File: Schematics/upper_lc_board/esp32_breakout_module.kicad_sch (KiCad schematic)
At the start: 28 parts, among them J1 USB_C_Female_USB2_Small, Q4 2N7002, SW1 SW_ESP_BOOT_MODE, SW2 SW_ESP_RESET, U1 ESP32-S3-WROOM-1-N16, U2 ISO1044BDR

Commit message: final upper control board
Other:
- moved on the sheet: C4, SW1, SW2

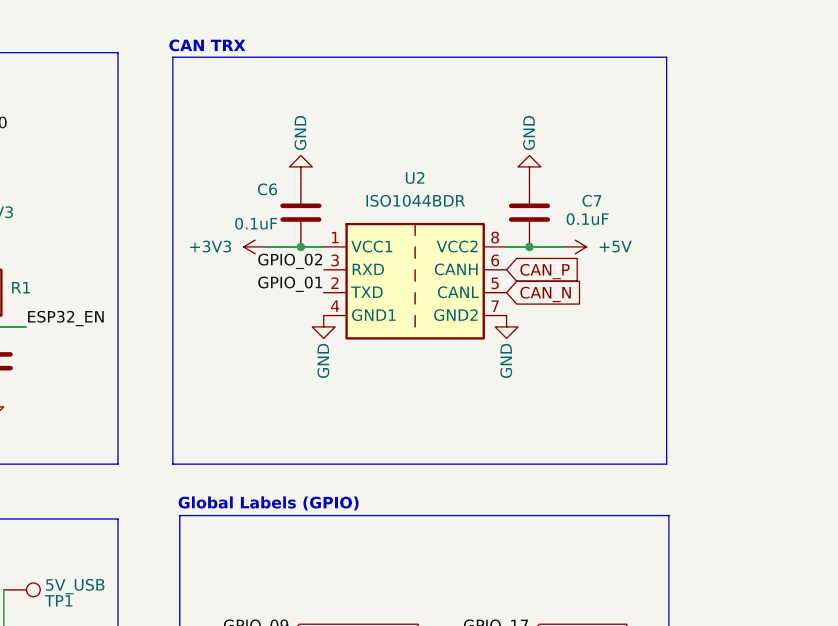
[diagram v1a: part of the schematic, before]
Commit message: final upper control board in cart, fixed HALL connector
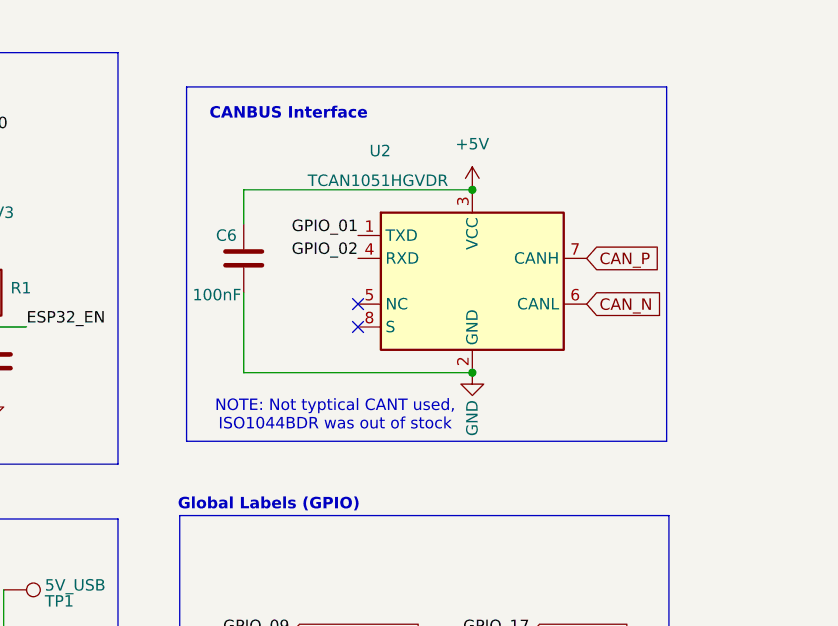
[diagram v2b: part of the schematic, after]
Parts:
- removed C7: 0.1uF, Capacitor_SMD:C_0603_1608Metric, symbol Device:C
- removed U2: ISO1044BDR, ul_ISO1044BDR:SOIC127P600X175-8N, symbol Interface_CAN_LIN:ISO1044BD
- added U2: TCAN1051HGVDR, ul_ISO1044BDR:SOIC_1044BDR_TEX, symbol Interface_CAN_LIN:TCAN330
- C6: value 0.1uF -> 100nF
- U1: Digikey (none) -> 5407-ESP32-S3-WROOM-1-N16CT-ND; LCSC C2913199 -> (none)
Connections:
- net +3V3: no longer C6.1
- net +5V: now also C6.2, U2.3 (VCC)
- net CAN_N: now also U2.6 (CANL)
- net CAN_P: now also U2.7 (CANH)
- net GND: now also C6.1, U2.2 (GND); no longer C6.2
- net GPIO_01: now also U2.1 (TXD)
- net GPIO_02: now also U2.4 (RXD)
- no-connect marks 13 -> 15
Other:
- note added: "CANBUS Interface"
- note added: "NOTE: Not typtical CANT used, ISO1044BDR was out of stock"
- note removed: "CAN TRX"

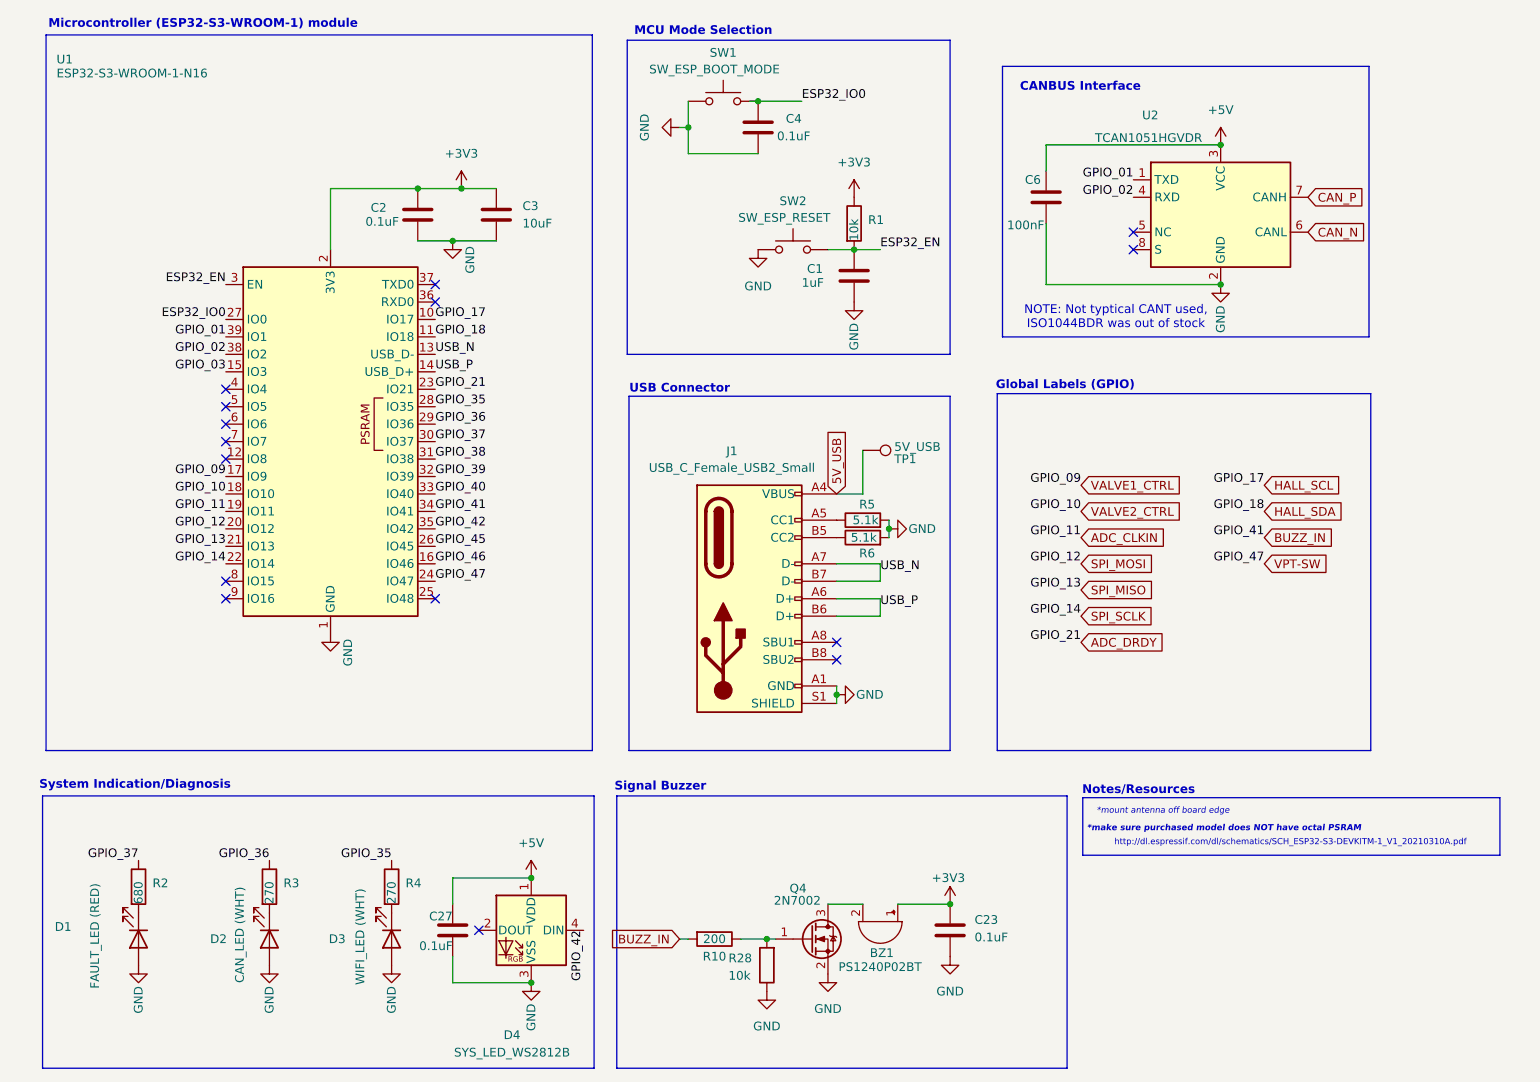
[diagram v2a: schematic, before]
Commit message: added 24V sensing to upper board
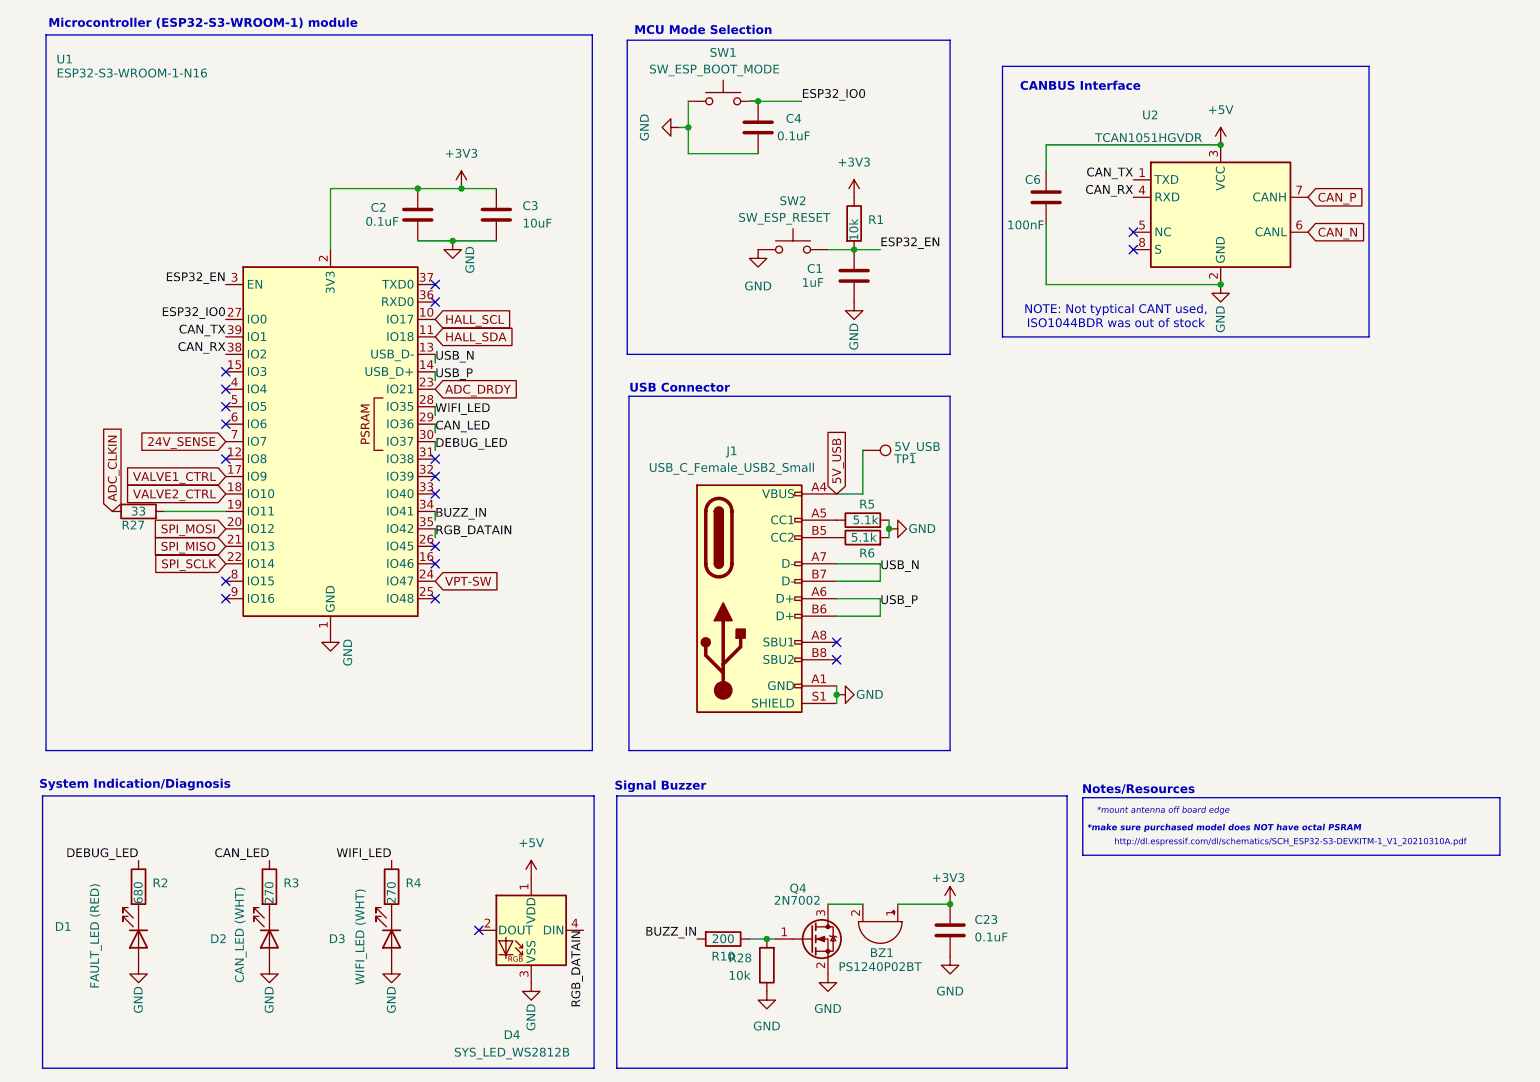
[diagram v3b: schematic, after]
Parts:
- removed C27: 0.1uF, Capacitor_SMD:C_0603_1608Metric, symbol Device:C
- added R27: 33, Resistor_SMD:R_0603_1608Metric, symbol Device:R
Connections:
- net ADC_CLKIN: now also R27.1; no longer U1.19 (IO11)
- net 24V_SENSE: now reaches U1.7 (IO7)
- net GPIO_01 renamed CAN_TX
- net GPIO_02 renamed CAN_RX
- net GPIO_03: no longer names the net of U1.15 (IO3)
- net GPIO_35 renamed WIFI_LED
- net GPIO_36 renamed CAN_LED
- net GPIO_37 renamed DEBUG_LED
- net GPIO_38: no longer names the net of U1.31 (IO38)
- net GPIO_39: no longer names the net of U1.32 (IO39)
- net GPIO_40: no longer names the net of U1.33 (IO40)
- net GPIO_42 renamed RGB_DATAIN
- net GPIO_45: no longer names the net of U1.26 (IO45)
- net GPIO_46: no longer names the net of U1.16 (IO46)
- new net: R27.2, U1.19 (IO11)
- no-connect marks 15 -> 20
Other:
- note removed: "Global Labels (GPIO)"
- moved on the sheet: R10

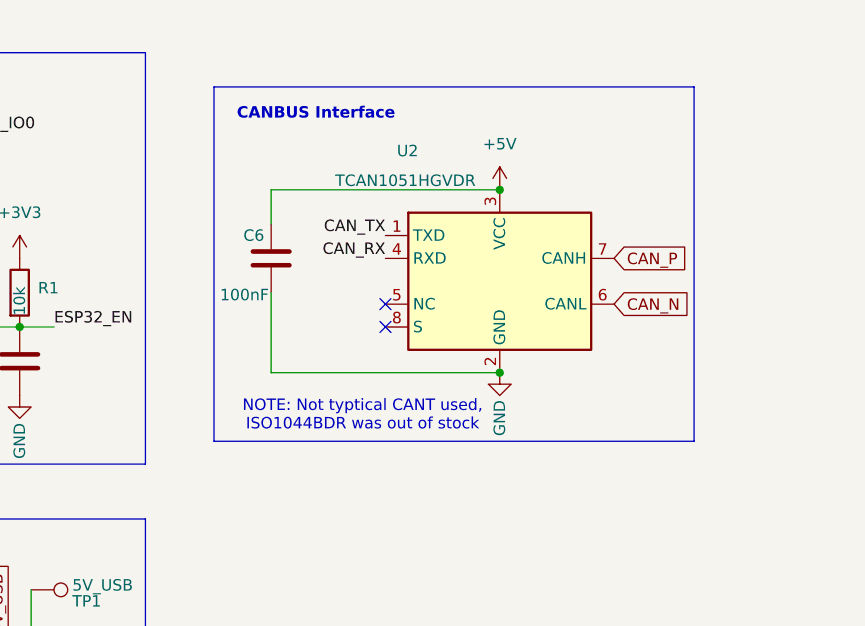
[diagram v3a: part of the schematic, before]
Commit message: add board-specifc READMEs (TODO), cleanup schematic titles
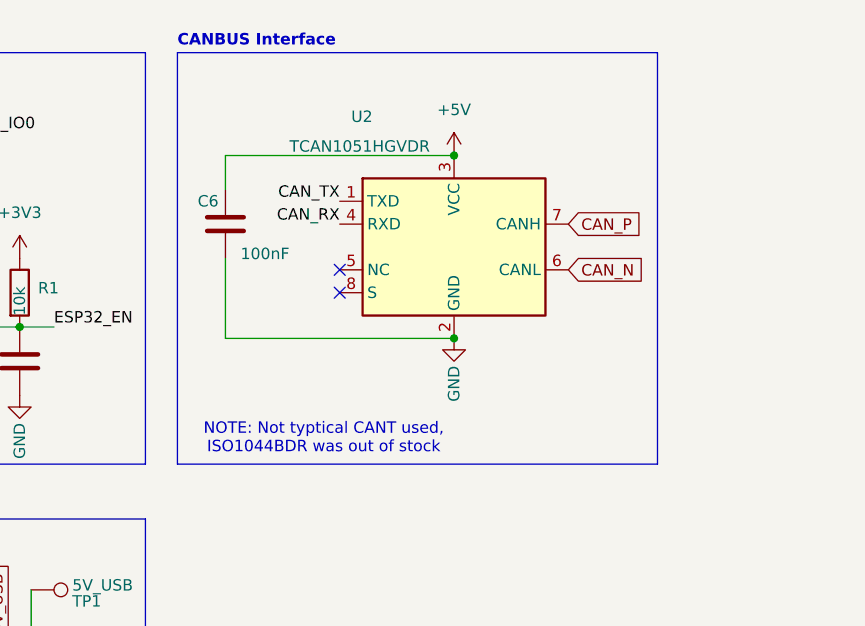
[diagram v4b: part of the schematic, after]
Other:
- title: ESP32-S3 Breakout Module -> ESP32-S3 Breakout Circuitry
- moved on the sheet: C6, U2
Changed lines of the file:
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@@
 	(paper "A4")
 	(title_block
-		(title "ESP32-S3 Breakout Module")
-		(rev "B")
+		(title "ESP32-S3 Breakout Circuitry")
 		(company "Queen's Rocket Engineering Team")
-		(comment 1 "Upper Control Board V2")
-		(comment 2 "Jeevan Sanchez")
+		(comment 1 "Contributors: Jeevan Sanchez, Tristan Alderson")
+		(comment 2 "PEGASUS - Upper Control Board")
 	)
 	(junction
@@
 	)
 	(junction
-		(at 187.96 64.77)
+		(at 182.88 60.96)
 		(diameter 0)
 		(color 0 0 0 0)
@@
 	)
 	(junction
-		(at 187.96 44.45)
+		(at 182.88 40.64)
 		(diameter 0)
 		(color 0 0 0 0)
@@
 	)
 	(no_connect
-		(at 175.26 57.15)
+		(at 170.18 53.34)
 	)
 	(no_connect
@@
 	)
 	(no_connect
-		(at 175.26 59.69)
+		(at 170.18 55.88)
 	)
 	(no_connect
@@
 		(at 43.18 82.55)
 	)
-	(polyline
-		(pts
-			(xy 156.21 33.02) (xy 156.21 72.39)
-		)
-		(stroke
-			(width 0)
-			(type default)
-		)
-	)
 	(wire
 		(pts
-			(xy 162.56 64.77) (xy 187.96 64.77)
+			(xy 157.48 60.96) (xy 182.88 60.96)
 		)
 		(stroke
@@
 		)
 	)
-	(polyline
-		(pts
-			(xy 209.55 72.39) (xy 209.55 33.02)
-		)
-		(stroke
-			(width 0)
-			(type default)
-		)
-	)
 	(wire
 		(pts
@@
 		)
 	)
-	(polyline
-		(pts
-			(xy 209.55 72.39) (xy 156.21 72.39)
-		)
-		(stroke
-			(width 0)
-			(type default)
-		)
-	)
 	(wire
 		(pts
@@
 	(wire
 		(pts
-			(xy 162.56 55.88) (xy 162.56 64.77)
+			(xy 157.48 52.07) (xy 157.48 60.96)
 		)
 		(stroke
@@
 		)
 	)
-	(polyline
-		(pts
-			(xy 156.21 33.02) (xy 209.55 33.02)
-		)
-		(stroke
-			(width 0)
-			(type default)
-		)
-	)
 	(wire
 		(pts
@@
 	(wire
 		(pts
-			(xy 162.56 44.45) (xy 187.96 44.45)
+			(xy 157.48 40.64) (xy 182.88 40.64)
 		)
 		(stroke
@@
 	(wire
 		(pts
-			(xy 162.56 48.26) (xy 162.56 44.45)
+			(xy 157.48 44.45) (xy 157.48 40.64)
 		)
 		(stroke
@@
 	)
 	(rectangle
+		(start 152.146 29.21)
+		(end 205.486 74.93)
+		(stroke
+			(width 0)
+			(type default)
+			(color 0 0 0 1)
+		)
+		(fill
+			(type none)
+		)
+	)
+	(rectangle
 		(start 17.018 28.448)
 		(end 96.52 132.588)
@@
 	(text "CANBUS Interface"
 		(exclude_from_sim no)
-		(at 158.75 36.83 0)
+		(at 152.146 28.702 0)
 		(effects
 			(font
@@
 				(thickness 0.254)
 				(bold yes)
+				(color 0 0 0 1)
 			)
 			(justify left bottom)
@@
 	(text "NOTE: Not typtical CANT used, \nISO1044BDR was out of stock"
 		(exclude_from_sim no)
-		(at 172.72 69.596 0)
+		(at 168.402 72.136 0)
 		(effects
 			(font
@@
 	)
 	(label "CAN_RX"
-		(at 175.26 52.07 180)
+		(at 170.18 48.26 180)
 		(fields_autoplaced yes)
 		(effects
@@
 	)
 	(label "CAN_TX"
-		(at 175.26 49.53 180)
+		(at 170.18 45.72 180)
 		(fields_autoplaced yes)
 		(effects
@@
 	(global_label "CAN_P"
 		(shape input)
-		(at 200.66 52.07 0)
+		(at 195.58 48.26 0)
 		(fields_autoplaced yes)
 		(effects
@@
 		)
 		(property "Intersheetrefs" "${INTERSHEET_REFS}"
-			(at 209.5719 52.07 0)
+			(at 204.4919 48.26 0)
 			(effects
 				(font
@@
 	(global_label "CAN_N"
 		(shape input)
-		(at 200.66 57.15 0)
+		(at 195.58 53.34 0)
 		(fields_autoplaced yes)
 		(effects
@@
 		)
 		(property "Intersheetrefs" "${INTERSHEET_REFS}"
-			(at 209.6324 57.15 0)
+			(at 204.5524 53.34 0)
 			(effects
 				(font
@@
 	(symbol
 		(lib_id "Device:C")
-		(at 162.56 52.07 180)
+		(at 157.48 48.26 180)
 		(unit 1)
 		(exclude_from_sim no)
@@
 		(dnp no)
 		(property "Reference" "C6"
-			(at 161.798 49.53 0)
+			(at 156.718 45.72 0)
 			(effects
 				(font
@@
 		)
 		(property "Value" "100nF"
-			(at 162.306 56.134 0)
+			(at 164.592 51.562 0)
 			(effects
 				(font
@@
 		)
 		(property "Footprint" "Capacitor_SMD:C_0603_1608Metric"
-			(at 161.5948 48.26 0)
+			(at 156.5148 44.45 0)
 			(effects
 				(font
@@
 		)
 		(property "Datasheet" "~"
-			(at 162.56 52.07 0)
+			(at 157.48 48.26 0)
 			(effects
 				(font
@@
 		)
 		(property "Description" "Unpolarized capacitor"
-			(at 162.56 52.07 0)
+			(at 157.48 48.26 0)
 			(effects
 				(font
@@
 		)
 		(property "LCSC" "C14663"
-			(at 162.56 52.07 0)
+			(at 157.48 48.26 0)
 			(effects
 				(font
@@
 	(symbol
 		(lib_id "power:GND")
-		(at 187.96 64.77 0)
+		(at 182.88 60.96 0)
 		(unit 1)
 		(exclude_from_sim no)
@@
 		(dnp no)
 		(property "Reference" "#PWR015"
-			(at 187.96 71.12 0)
+			(at 182.88 67.31 0)
 			(effects
 				(font
@@
 		)
 		(property "Value" "GND"
-			(at 187.96 67.818 90)
+			(at 182.88 64.008 90)
 			(effects
 				(font
@@
 		)
 		(property "Footprint" ""
-			(at 187.96 64.77 0)
+			(at 182.88 60.96 0)
 			(effects
 				(font
@@
 		)
 		(property "Datasheet" ""
-			(at 187.96 64.77 0)
+			(at 182.88 60.96 0)
 			(effects
 				(font
@@
 		)
 		(property "Description" "Power symbol creates a global label with name \"GND\" , ground"
-			(at 187.96 64.77 0)
+			(at 182.88 60.96 0)
 			(effects
 				(font
@@
 	(symbol
 		(lib_id "power:+5V")
-		(at 187.96 44.45 0)
+		(at 182.88 40.64 0)
 		(unit 1)
 		(exclude_from_sim no)
@@
 		(fields_autoplaced yes)
 		(property "Reference" "#PWR016"
-			(at 187.96 48.26 0)
+			(at 182.88 44.45 0)
 			(effects
 				(font
@@
 		)
 		(property "Value" "+5V"
-			(at 187.96 39.37 0)
+			(at 182.88 35.56 0)
 			(effects
 				(font
@@
 		)
 		(property "Footprint" ""
-			(at 187.96 44.45 0)
+			(at 182.88 40.64 0)
 			(effects
 				(font
@@
 		)
 		(property "Datasheet" ""
-			(at 187.96 44.45 0)
+			(at 182.88 40.64 0)
 			(effects
 				(font
@@
 		)
 		(property "Description" "Power symbol creates a global label with name \"+5V\""
-			(at 187.96 44.45 0)
+			(at 182.88 40.64 0)
 			(effects
 				(font
@@
 	(symbol
 		(lib_id "Interface_CAN_LIN:TCAN330")
-		(at 187.96 54.61 0)
+		(at 182.88 50.8 0)
 		(unit 1)
 		(exclude_from_sim no)
@@
 		(dnp no)
 		(property "Reference" "U2"
-			(at 176.53 40.132 0)
+			(at 171.45 36.322 0)
 			(effects
 				(font
@@
 		)
 		(property "Value" "TCAN1051HGVDR"
-			(at 169.672 43.434 0)
+			(at 164.592 39.624 0)
 			(effects
 				(font
@@
 		)
 		(property "Footprint" "ul_ISO1044BDR:SOIC_1044BDR_TEX"
-			(at 187.96 67.31 0)
+			(at 182.88 63.5 0)
 			(effects
 				(font
@@
 		)
 		(property "Datasheet" "{KIPRJMOD}/../../Datasheets/tcan1051h.pdf"
-			(at 187.96 54.61 0)
+			(at 182.88 50.8 0)
 			(effects
 				(font
@@
 		)
 		(property "Description" ""
-			(at 187.96 54.61 0)
+			(at 182.88 50.8 0)
 			(effects
 				(font
@@
 		)
 		(property "Digikey" "296-44225-1-ND"
-			(at 187.96 54.61 0)
+			(at 182.88 50.8 0)
 			(effects
 				(font

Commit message: add ed pinouts
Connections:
- net BUZZ_IN renamed BUZZ_EN
- net SPI_MISO renamed ADC_MISO
- net SPI_MOSI renamed ADC_MOSI
- net SPI_SCLK renamed ADC_SCLK
- net VALVE1_CTRL renamed SOL1_EN
- net VALVE2_CTRL renamed SOL2_EN
- net VPT-SW renamed VPT_EN
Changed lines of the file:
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@@
 		)
 	)
-	(label "BUZZ_IN"
+	(label "BUZZ_EN"
 		(at 73.66 99.06 0)
 		(fields_autoplaced yes)
@@
 		)
 	)
-	(label "BUZZ_IN"
+	(label "BUZZ_EN"
 		(at 111.76 160.02 180)
 		(fields_autoplaced yes)
@@
 		)
 	)
-	(global_label "VALVE1_CTRL"
+	(global_label "SOL1_EN"
 		(shape input)
 		(at 43.18 92.71 180)
@@
 		)
 		(property "Intersheetrefs" "${INTERSHEET_REFS}"
-			(at 28.0391 92.71 0)
+			(at 31.9701 92.71 0)
 			(effects
 				(font
@@
 		)
 	)
-	(global_label "SPI_MOSI"
+	(global_label "ADC_MOSI"
 		(shape input)
 		(at 43.18 100.33 180)
@@
 		)
 		(property "Intersheetrefs" "${INTERSHEET_REFS}"
-			(at 31.5467 100.33 0)
+			(at 31.0024 100.33 0)
 			(effects
 				(font
@@
 		)
 	)
-	(global_label "VPT-SW"
+	(global_label "VPT_EN"
 		(shape input)
 		(at 73.66 107.95 0)
@@
 		)
 		(property "Intersheetrefs" "${INTERSHEET_REFS}"
-			(at 84.2047 107.95 0)
-			(effects
-				(font
-					(size 1.27 1.27)
-				)
-				(justify left)
-				(hide yes)
-			)
-		)
-	)
-	(global_label "SPI_MISO"
+			(at 83.4185 107.95 0)
+			(effects
+				(font
+					(size 1.27 1.27)
+				)
+				(justify left)
+				(hide yes)
+			)
+		)
+	)
+	(global_label "ADC_MISO"
 		(shape input)
 		(at 43.18 102.87 180)
@@
 		)
 		(property "Intersheetrefs" "${INTERSHEET_REFS}"
-			(at 31.5467 102.87 0)
+			(at 31.0024 102.87 0)
 			(effects
 				(font
@@
 		)
 	)
-	(global_label "VALVE2_CTRL"
+	(global_label "SOL2_EN"
 		(shape input)
 		(at 43.18 95.25 180)
@@
 		)
 		(property "Intersheetrefs" "${INTERSHEET_REFS}"
-			(at 28.0391 95.25 0)
+			(at 31.9701 95.25 0)
 			(effects
 				(font
@@
 		)
 	)
-	(global_label "SPI_SCLK"
+	(global_label "ADC_SCLK"
 		(shape input)
 		(at 43.18 105.41 180)
@@
 		)
 		(property "Intersheetrefs" "${INTERSHEET_REFS}"
-			(at 31.3653 105.41 0)
-			(effects
-				(font
+			(at 30.821 105.41 0)
+			(effects
+				(font
